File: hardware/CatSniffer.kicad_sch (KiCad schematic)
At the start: 94 parts, among them J1 Antenna, J2 Conn_01x06_Female, J3 Conn_01x06_Female, P1 USB_C_Plug_USB2.0, SW1 SW, U1 AP2112K-3.3, U2 RFSW8006QTR7, U3 ATSAMD21E18A, U4 0900PC15A0036, U5 0900FM15D0039, U6 PE42421, U7 SX1262IMLTRT, U8 CC1352P1F3RGZT, Y1 48MHz, Y2 32.768kHz, Y3 32Mhz

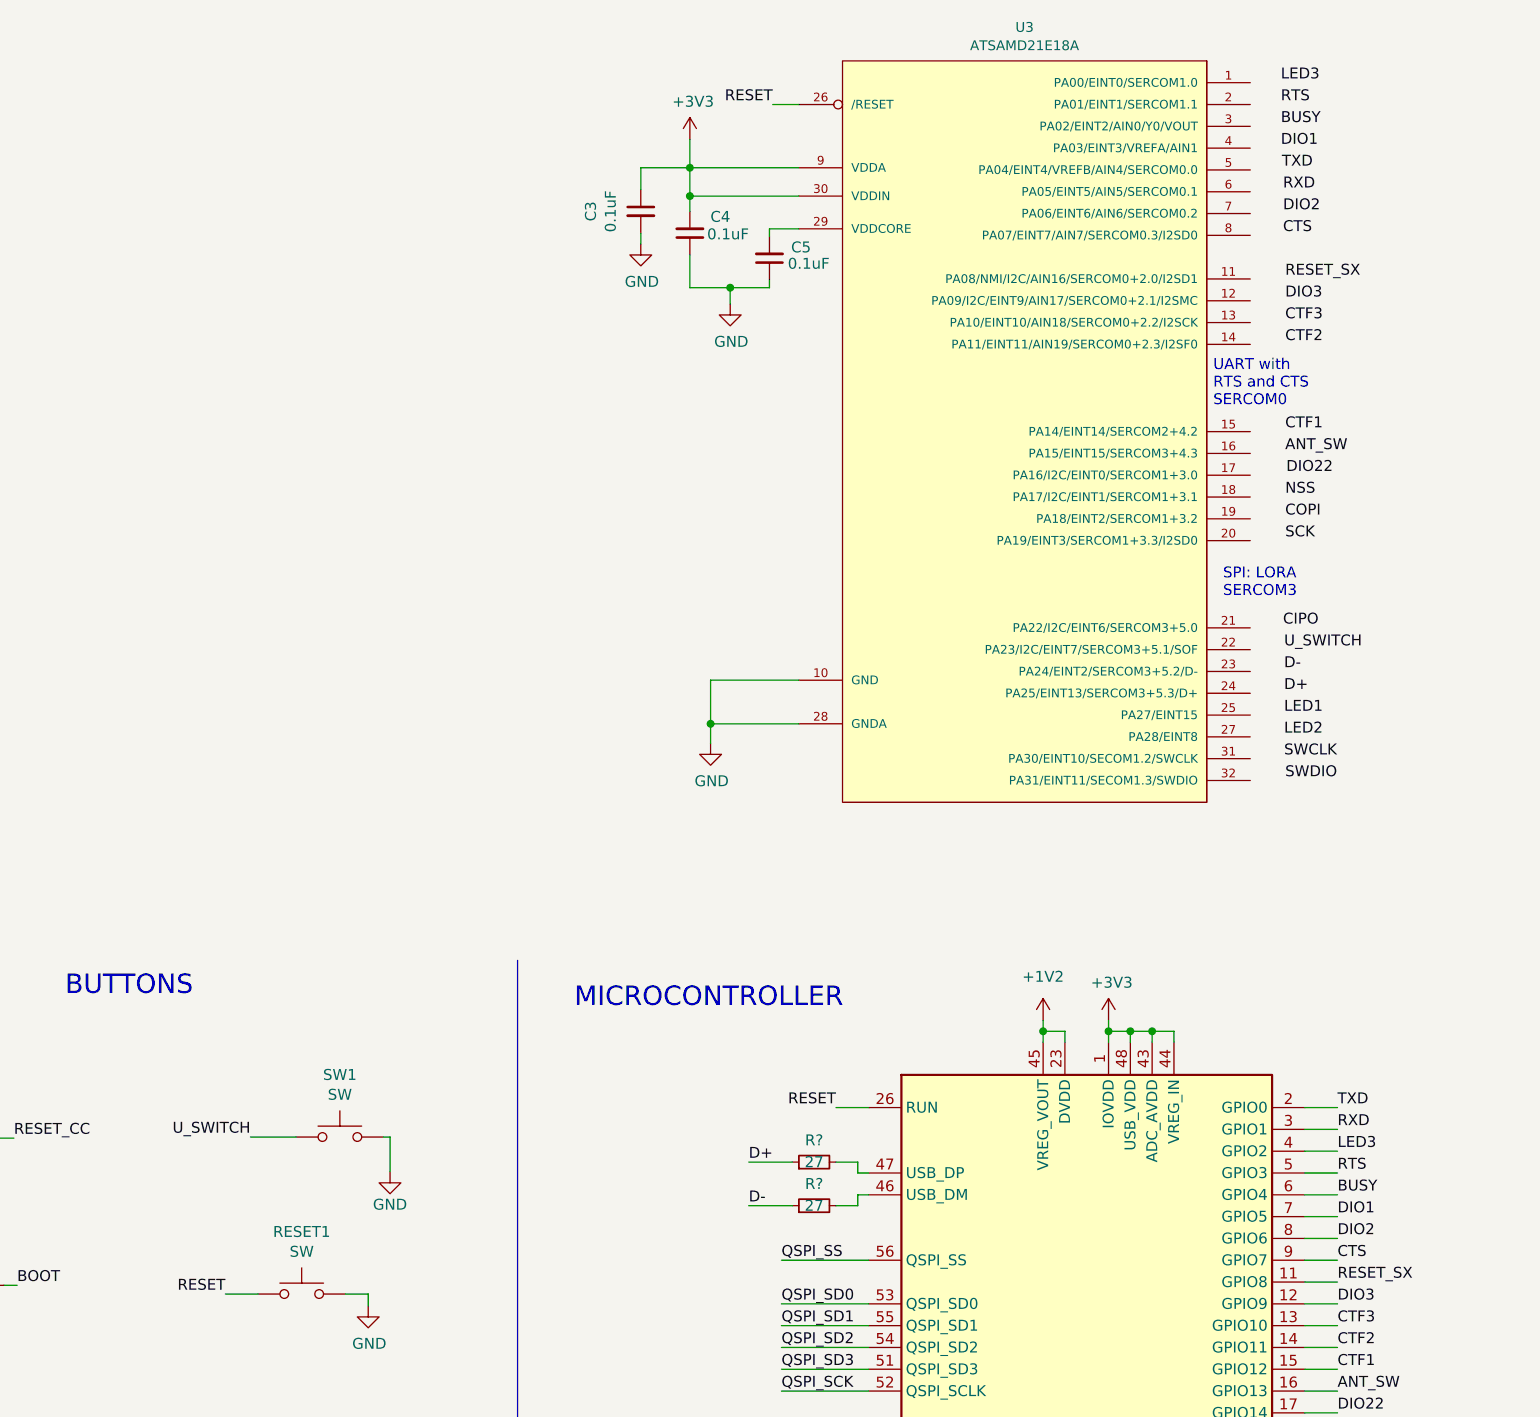
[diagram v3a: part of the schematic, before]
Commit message: Add boot rp2040, add CTS and RTS serial
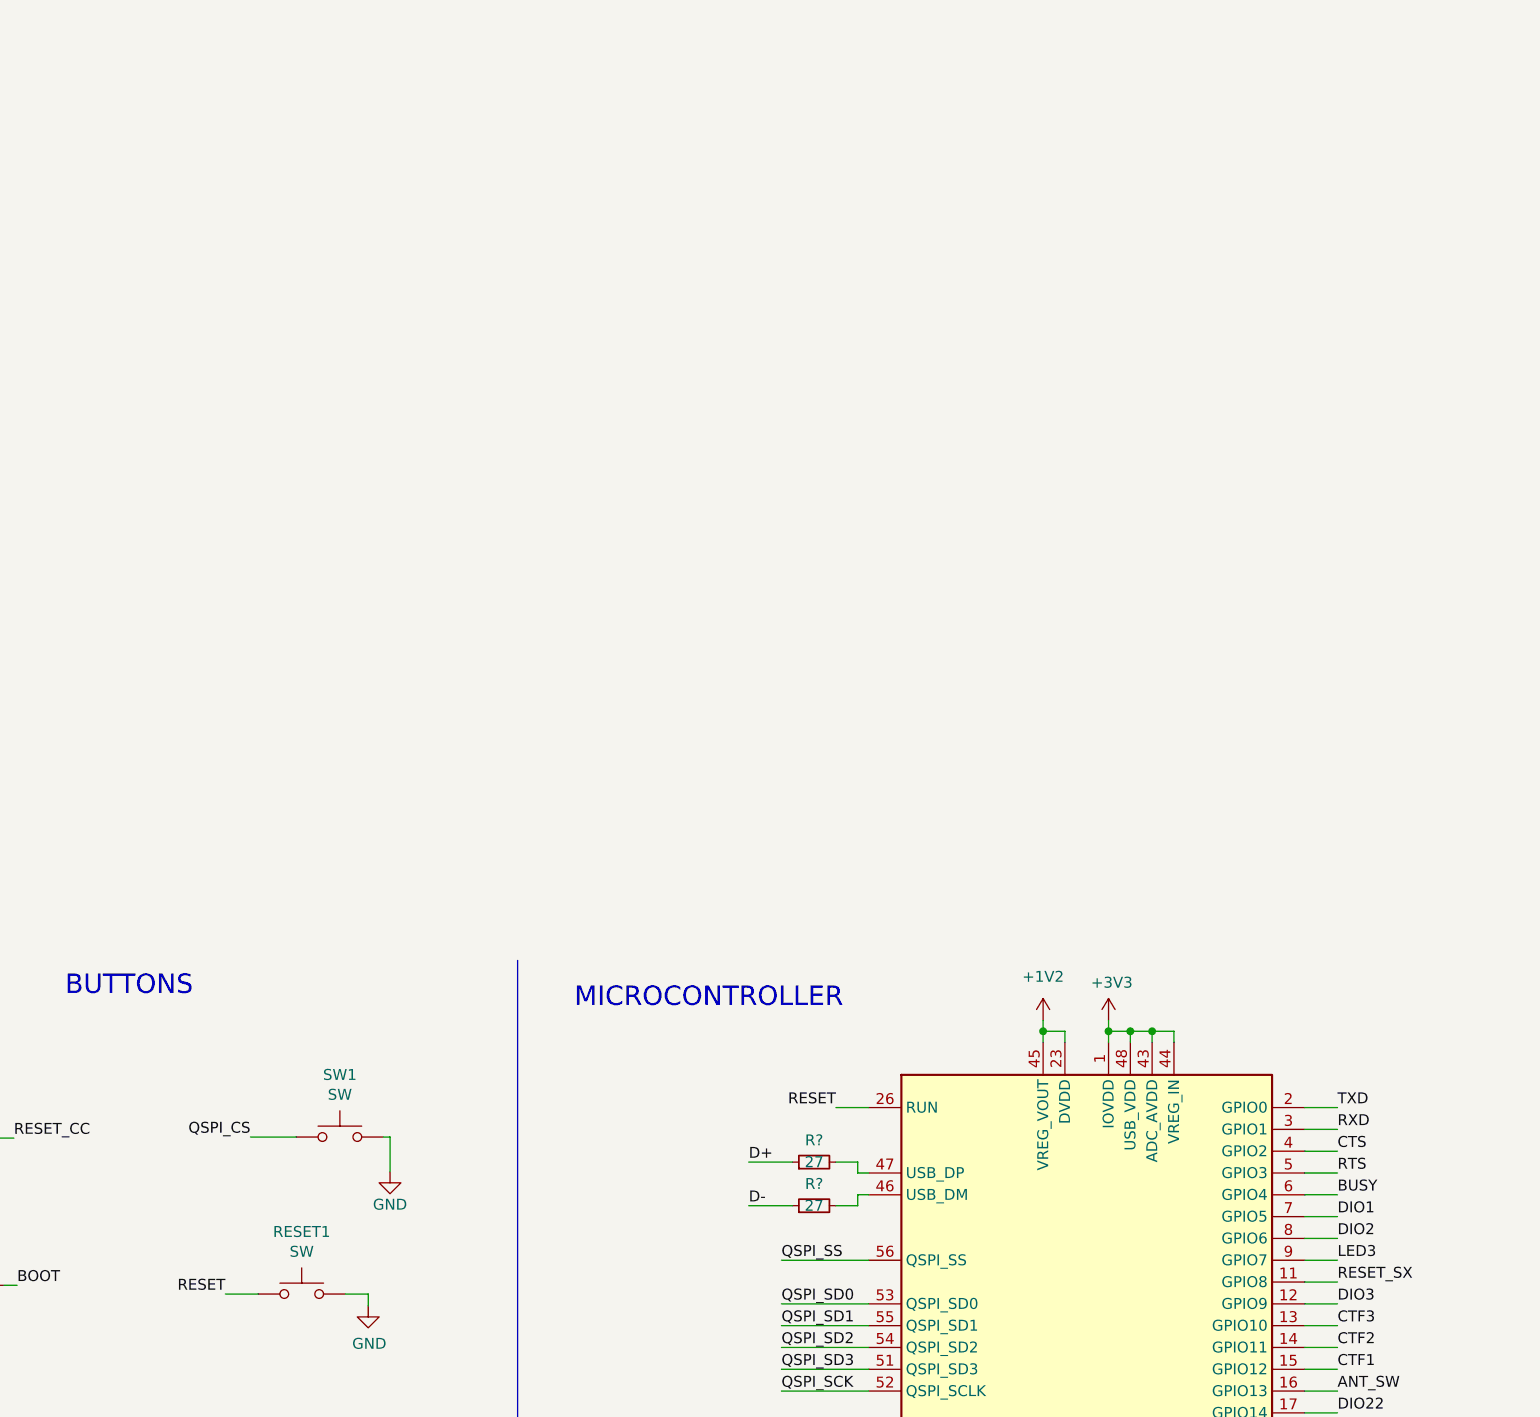
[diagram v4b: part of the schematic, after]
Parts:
- removed C3, C4, C5: 0.1uF, Capacitor_SMD:C_0603_1608Metric, symbol CatSniffer-rescue:C_Small-Device-CatStick-rescue-CatSniffer-rescue
- removed U3: ATSAMD21E18A, Package_DFN_QFN:QFN-32-1EP_5x5mm_P0.5mm_EP3.65x3.65mm, symbol CatSniffer-rescue:ATSAMD21E18A-electroniccats-CatStick-rescue-CatSniffer-rescue
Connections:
- net BOOT: now also U?.4 (GPIO2); no longer U?.9 (GPIO7)
- net LED3: now also U?.9 (GPIO7); no longer U?.4 (GPIO2)
- net U_SWITCH: no longer SW1.1
- new net QSPI_CS: SW1.1
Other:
- note removed: "SPI: LORA SERCOM3"
- note removed: "UART with RTS and CTS SERCOM0"

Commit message: BOM and schematic
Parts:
- added C37: 0.1uF, Capacitor_SMD:C_0603_1608Metric, symbol Device:C_Small
- C11: renamed from C1; LCSC# C108343 -> C15849
- C12: renamed from C13; Mouser# 81-GRM155R61H104KE9D -> (none)
- C13: renamed from C2; LCSC# C14663 -> C282519; manf# CC0603KRX7R9BB104 -> GRM155R62A104ME14D
- C15, C16: Mouser# 81-GRM155R61H104KE9D -> (none)
- C19, C25: renamed from C?; footprint (none) -> Capacitor_SMD:C_0603_1608Metric; LCSC# (none) -> C15849; manf# (none) -> 0603F105M500NT; provedor (none) -> LCSC
- C20, C22: renamed from C?; footprint (none) -> Capacitor_SMD:C_0603_1608Metric; LCSC# (none) -> C92670; manf# (none) -> 0603CG270J500NT; provedor (none) -> LCSC
- C21, C24, C26, C27, C28, C29, C32, C35, C36: renamed from C?; footprint (none) -> Capacitor_SMD:C_0603_1608Metric; LCSC# (none) -> C282519; manf# (none) -> GRM155R62A104ME14D; provedor (none) -> LCSC
- C23: renamed from C29; LCSC# C14663 -> C282519; manf# CC0603KRX7R9BB104 -> GRM155R62A104ME14D
- C30: renamed from C24; LCSC# C14663 -> C282519; manf# CC0603KRX7R9BB104 -> GRM155R62A104ME14D
- C33: renamed from C21; LCSC# C14663 -> C282519; manf# CC0603KRX7R9BB104 -> GRM155R62A104ME14D
- C5: renamed from C32; Mouser# 81-GRM155R61H104KE9D -> (none)
- C6: renamed from C37; LCSC# C108343 -> C15849
- C7: renamed from C10; Mouser# 81-GRM155R61H104KE9D -> (none)
- C8: renamed from C11; Mouser# 81-GRM155R61H104KE9D -> (none)
- C9: renamed from C12; Mouser# 81-GRM155R61H104KE9D -> (none)
- F1: Mouser# (none) -> 594-MFU0805FF00500P1
- R5, R6: renamed from R?; footprint (none) -> Resistor_SMD:R_0603_1608Metric; LCSC# (none) -> C403464; manf# (none) -> ERJ3GEYJ270V; provedor (none) -> LCSC
- R7: renamed from R?; footprint (none) -> Resistor_SMD:R_0603_1608Metric; LCSC# (none) -> C112433; manf# (none) -> WR06X1001FTL; provedor (none) -> LCSC
- R8: renamed from R?; footprint (none) -> Resistor_SMD:R_0603_1608Metric; LCSC# (none) -> C169849; manf# (none) -> ERJ3GEYJ103V; provedor (none) -> LCSC
- U2: renamed from U1; Mouser# 621-AP7365-33WG-7 -> 621-AP7347DQ-33W5-7; manf# AP7365-33WG-7 -> AP7347DQ-33W5-7
- U5: renamed from U?; LCSC# (none) -> C2040; manf# (none) -> RP2040; provedor (none) -> LCSC
- U7: renamed from U?; Mouser# (none) -> 454-W25Q16JVUUIQTR; manf# (none) -> W25Q16JVUUIQ TR; provedor (none) -> Mouser
- U8: renamed from U6; Mouser# (none) -> 81-PE42421SCAA-Z
- Y3: renamed from Y?; footprint (none) -> Crystal:Crystal_SMD_5032-2Pin_5.0x3.2mm; LCSC# (none) -> C709001; manf# (none) -> CM4012M00020T8188026; provedor (none) -> LSCS
- renumbered C19 to C1, C14 to C10, C17 to C14, C27 to C17, C23 to C18, C18 to C2, C34 to C3, C33 to C31, C22 to C34, C6 to C38, C8 to C39, C36 to C4, C7 to C40, C35 to C41, C20 to C42, C31 to C43, C26 to C44, C9 to C45, C25 to C46, D4 to D1, D3 to D2, D2 to D3, D1 to D4, J3 to J1, J1 to J3, L5 to L3, L3 to L5, R9 to R1, R4 to R10, R3 to R11, R8 to R12, R7 to R13, R6 to R2, R1 to R3, R2 to R4, R5 to R9, U8 to U1, U4 to U3, U7 to U4, U5 to U6, U2 to U9, Y3 to Y4
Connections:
- net QSPI_SS is gone; now on net QSPI_CS: R8.2, U5.56 (QSPI_SS), U7.1 (~{CS})
- net +3V3: now also C37.1
- net ANT_SW: now also U5.31 (GPIO20); no longer U5.16 (GPIO13)
- net CIPO: now also U5.11 (GPIO8); no longer U5.27 (GPIO16)
- net COPI: now also U5.9 (GPIO7); no longer U5.30 (GPIO19)
- net CTF1: now also U5.30 (GPIO19); no longer U5.15 (GPIO12)
- net CTF2: now also U5.29 (GPIO18); no longer U5.14 (GPIO11)
- net DIO2: now also U5.35 (GPIO23); no longer U5.8 (GPIO6)
- net DIO22: now also U5.32 (GPIO21); no longer U5.17 (GPIO14)
- net DIO3: now also U5.37 (GPIO25); no longer U5.12 (GPIO9)
- net GND: now also C37.2
- net LED1: now also U5.27 (GPIO16); no longer U5.31 (GPIO20)
- net LED2: now also U5.28 (GPIO17); no longer U5.32 (GPIO21)
- net LED3: now also U5.38 (GPIO26_ADC0); no longer U5.9 (GPIO7)
- net NSS: now also U5.12 (GPIO9); no longer U5.28 (GPIO17)
- net RESET_CC: now also U5.18 (GPIO15)
- net RESET_SX: now also U5.36 (GPIO24); no longer U5.11 (GPIO8)
- net SCK: now also U5.8 (GPIO6); no longer U5.29 (GPIO18)
- net U_SWITCH: now also U5.34 (GPIO22); no longer U5.18 (GPIO15)
- net cJTAG_TCK: now also U5.14 (GPIO11)
- net cJTAG_TMSC: now also U5.15 (GPIO12)
- net JTAG/TDI: now reaches U1.26 (DIO_16)
- net JTAG/TDI: now also U5.16 (GPIO13)
- net JTAG/TDO: now reaches U1.27 (DIO_17)
- net JTAG/TDO: now also U5.17 (GPIO14)
- no-connect marks 34 -> 28
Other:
- moved on the sheet: C1, C2, C3, C6, J1, U1, Y1, Y2

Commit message: change of components rp2040
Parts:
- removed C37: 0.1uF, Capacitor_SMD:C_0603_1608Metric, symbol Device:C_Small
- added C46: 0.1uF, Capacitor_SMD:C_0603_1608Metric, symbol Device:C_Small
- C1: renamed from C11; LCSC# C15849 -> C108343
- C2: renamed from C13; LCSC# C282519 -> C14663; manf# GRM155R62A104ME14D -> CC0603KRX7R9BB104
- C21: renamed from C33; LCSC# C282519 -> C14663; manf# GRM155R62A104ME14D -> CC0603KRX7R9BB104
- C24: renamed from C30; LCSC# C282519 -> C14663; manf# GRM155R62A104ME14D -> CC0603KRX7R9BB104
- C29: renamed from C23; LCSC# C282519 -> C14663; manf# GRM155R62A104ME14D -> CC0603KRX7R9BB104
- C3: renamed from C19; LCSC# C15849 -> C108343
- C30: renamed from C24; LCSC# C282519 -> C14663; manf# GRM155R62A104ME14D -> CC0603KRX7R9BB104
- C37: renamed from C6; LCSC# C15849 -> C108343
- C38: renamed from C25; LCSC# C15849 -> C108343
- C39: renamed from C26; LCSC# C282519 -> C14663; manf# GRM155R62A104ME14D -> CC0603KRX7R9BB104
- C40: renamed from C27; LCSC# C282519 -> C14663; manf# GRM155R62A104ME14D -> CC0603KRX7R9BB104
- C41: renamed from C28; LCSC# C282519 -> C14663; manf# GRM155R62A104ME14D -> CC0603KRX7R9BB104
- C42: renamed from C29; LCSC# C282519 -> C14663; manf# GRM155R62A104ME14D -> CC0603KRX7R9BB104
- C43: renamed from C32; LCSC# C282519 -> C14663; manf# GRM155R62A104ME14D -> CC0603KRX7R9BB104
- C44: renamed from C35; LCSC# C282519 -> C14663; manf# GRM155R62A104ME14D -> CC0603KRX7R9BB104
- C45: renamed from C36; LCSC# C282519 -> C14663; manf# GRM155R62A104ME14D -> CC0603KRX7R9BB104
- C5: renamed from C21; LCSC# C282519 -> C14663; manf# GRM155R62A104ME14D -> CC0603KRX7R9BB104
- U1: renamed from U2; Mouser# 621-AP7347DQ-33W5-7 -> 865-XC6210B332MR-G; manf# AP7347DQ-33W5-7 -> XC6210B332MR-G
- U9: renamed from U7; footprint Package_SO:SOIC-8_5.23x5.23mm_P1.27mm -> CatSniffer:W25Q16JVUUIQ
- Y4: renamed from Y3; provedor LSCS -> LCSC
- renumbered C7 to C10, C8 to C11, C9 to C12, C12 to C13, C10 to C14, C14 to C17, C2 to C18, C1 to C19, C42 to C20, C34 to C22, C18 to C23, C46 to C25, C44 to C26, C17 to C27, C22 to C28, C43 to C31, C5 to C32, C31 to C33, C3 to C34, C41 to C35, C4 to C36, C20 to C4, C38 to C6, C40 to C7, C39 to C8, C45 to C9, D4 to D1, D3 to D2, D2 to D3, D1 to D4, J3 to J1, J1 to J3, L5 to L3, L3 to L5, R3 to R1, R5 to R10, R6 to R11, R7 to R12, R8 to R13, R4 to R2, R11 to R3, R10 to R4, R9 to R5, R2 to R6, R13 to R7, R12 to R8, R1 to R9, U9 to U2, U5 to U3, U3 to U4, U6 to U5, U8 to U6, U4 to U7, U1 to U8, Y4 to Y3
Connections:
- net +3V3: now also C46.1
- net GND: now also C46.2
- net cJTAG_TCK: no longer U3.14 (GPIO11)
- net QSPI_CS renamed QSPI_SS
- new net JTAG/TCK: U3.14 (GPIO11)
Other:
- moved on the sheet: R13, U9

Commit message: change to rp2040
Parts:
- C28, C4: footprint Capacitor_SMD:C_0603_1608Metric -> Capacitor_SMD:C_0402_1005Metric; LCSC# C92670 -> (none); Mouser# (none) -> 81-GJM1555C1H270FB1D; manf# 0603CG270J500NT -> GJM1555C1H270FB01D; provedor LCSC -> Mouser
- C3, C38: footprint Capacitor_SMD:C_0603_1608Metric -> Capacitor_SMD:C_0402_1005Metric; LCSC# C108343 -> (none); Mouser# (none) -> 963-MAASA105CD7105MF; manf# 0603F105M500NT -> MAASA105CD7105MFCA01; provedor LCSC -> Mouser
- C30, C39, C40, C41, C42, C43, C44, C45, C46, C5: footprint Capacitor_SMD:C_0603_1608Metric -> Capacitor_SMD:C_0402_1005Metric; LCSC# C14663 -> (none); Mouser# (none) -> 963-MSAST105SB7104KF; manf# CC0603KRX7R9BB104 -> MSAST105SB7104KFNB25; provedor LCSC -> Mouser
- R10, R11: footprint Resistor_SMD:R_0603_1608Metric -> Resistor_SMD:R_0402_1005Metric; LCSC# C403464 -> (none); Mouser# (none) -> 755-ESR01MZPF27R0; manf# ERJ3GEYJ270V -> ESR01MZPF27R0; provedor LCSC -> Mouser
- R12: footprint Resistor_SMD:R_0603_1608Metric -> Resistor_SMD:R_0402_1005Metric; LCSC# C112433 -> (none); Mouser# (none) -> 594-MCS0402MD1001DE0; manf# WR06X1001FTL -> MCS0402MD1001DE000; provedor LCSC -> Mouser
- R13: footprint Resistor_SMD:R_0603_1608Metric -> Resistor_SMD:R_0402_1005Metric; LCSC# C169849 -> (none); Mouser# (none) -> 594-MCS04020D1002BE0; manf# ERJ3GEYJ103V -> MCS04020D1002BE000; provedor LCSC -> Mouser
